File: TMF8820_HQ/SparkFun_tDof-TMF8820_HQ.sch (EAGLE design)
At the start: 24 parts, among them J4 QWIIC_RIGHT_ANGLE, J5 QWIIC_RIGHT_ANGLE

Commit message: Adds default address to HQ boards, fixes some clearance issues
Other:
- note added: "Default Addres: 0x41"
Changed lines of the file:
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@@
 <text x="58.42" y="165.1" size="1.778" layer="97" font="vector">VCC Range: 2.7V - 3.3V
 I/O VCC Range: 1.62V - 3.3V</text>
+<text x="83.82" y="111.76" size="1.778" layer="97" font="vector">Default Addres: 0x41</text>
 </plain>
 <instances>

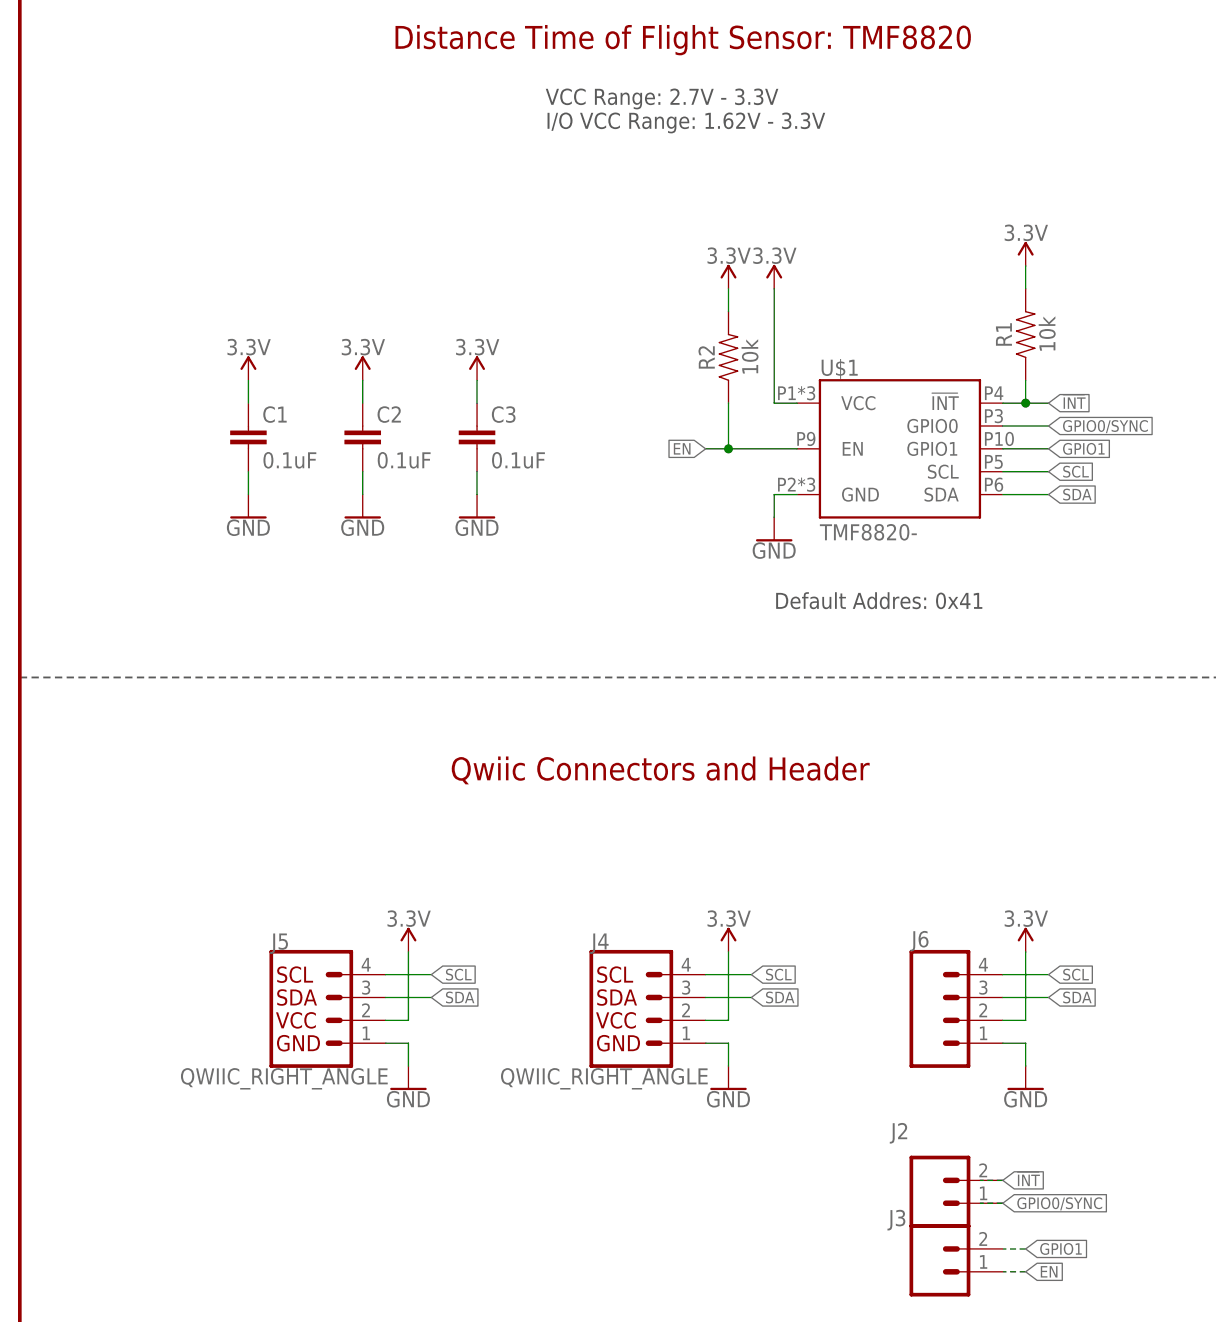
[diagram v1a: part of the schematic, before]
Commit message: Updates the TMF882X device in the library to have two variants of the two ICs
* Better silk labeling for the 8820 and 8820 HQ
* Adds new IC variants to both designs
* Adds default addresses to schematics
* Moves some traces and vias for better ground pour in the 8820 design
* Moves entire 8820 design to origin in board file
* Adds measure from center of qwiic connector to edge in 8820 design
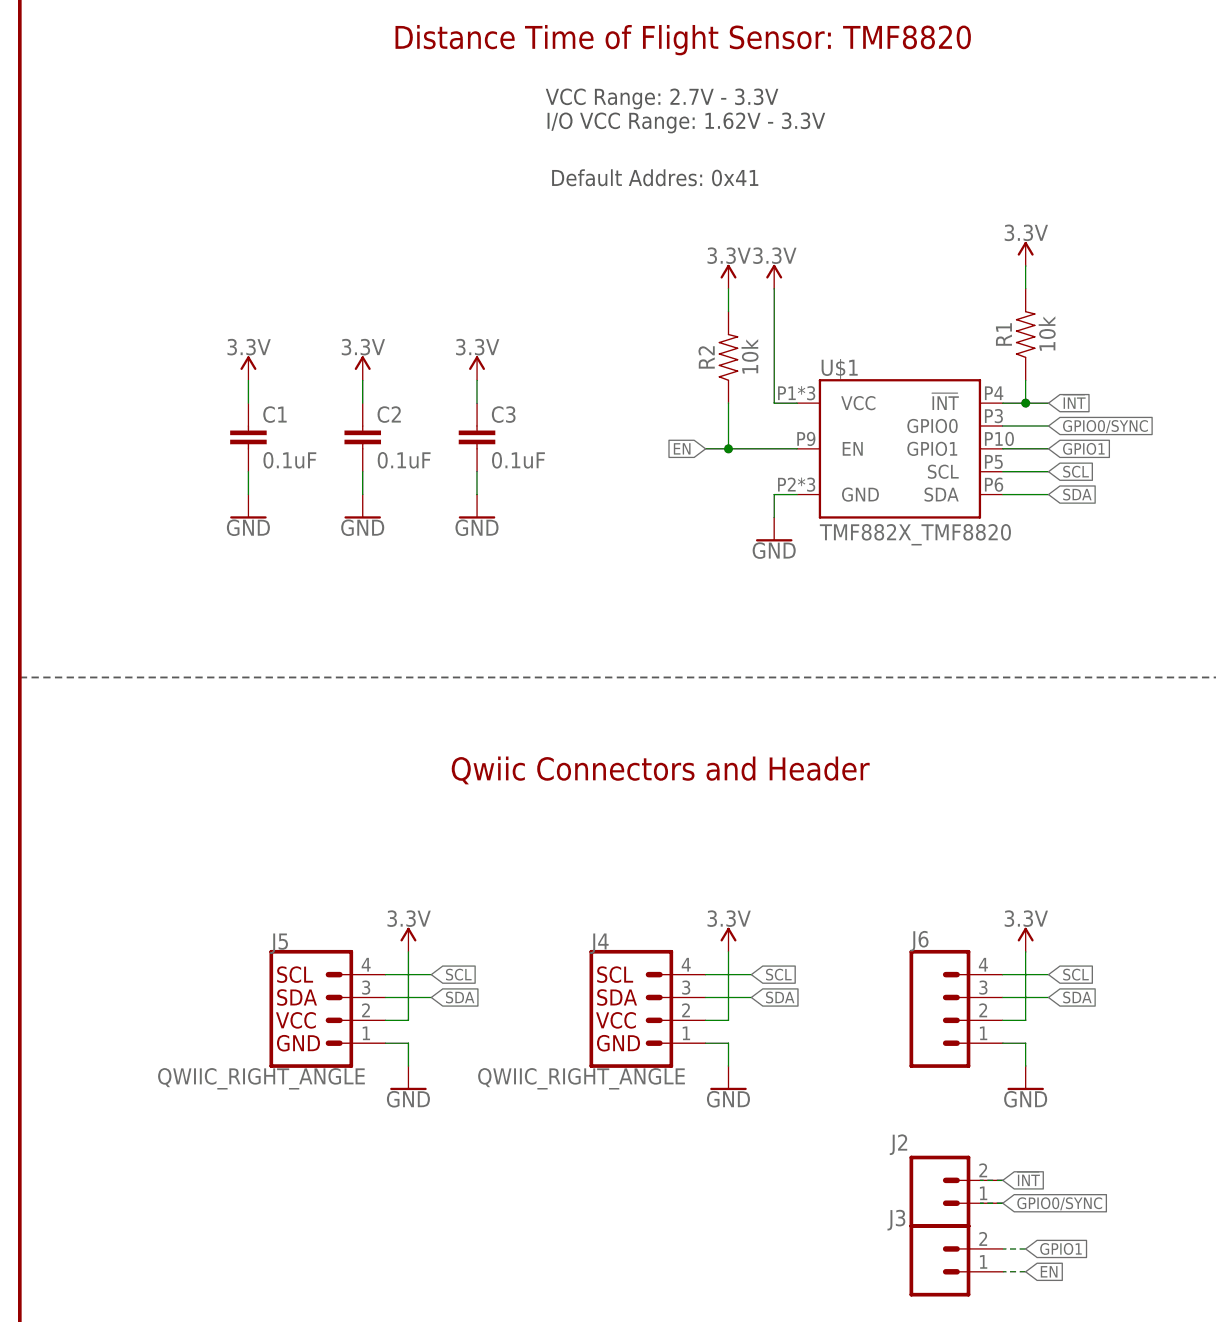
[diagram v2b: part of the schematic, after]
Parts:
- U$1: value TMF8820- -> TMF882X_TMF8820; device TMF882X:TMF8820- -> TMF882X:TMF882X_TMF8820
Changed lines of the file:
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@@
 <part name="I2C" library="SparkFun-Jumpers" deviceset="JUMPER-SMT_3_2-NC_TRACE" device="_SILK" package3d_urn="urn:adsk.eagle:package:39289/1" value="I2C_PU"/>
 <part name="SUPPLY10" library="SparkFun-PowerSymbols" deviceset="3.3V" device=""/>
-<part name="U$1" library="TMF882X" deviceset="TMF8820" device="-"/>
+<part name="U$1" library="TMF882X" deviceset="TMF882X" device="_TMF8820"/>
 <part name="C1" library="SparkFun-Capacitors" deviceset="0.1UF" device="-0402T-6.3V-10%-X7R" value="0.1uF"/>
 <part name="C2" library="SparkFun-Capacitors" deviceset="0.1UF" device="-0402T-6.3V-10%-X7R" value="0.1uF"/>
@@
 <text x="58.42" y="165.1" size="1.778" layer="97" font="vector">VCC Range: 2.7V - 3.3V
 I/O VCC Range: 1.62V - 3.3V</text>
-<text x="83.82" y="111.76" size="1.778" layer="97" font="vector">Default Addres: 0x41</text>
+<text x="58.928" y="158.75" size="1.778" layer="97" font="vector">Default Addres: 0x41</text>
 </plain>
 <instances>
@@
 <instance part="H8" gate="G$1" x="236.22" y="27.94" smashed="yes"/>
 <instance part="J4" gate="G$1" x="68.58" y="66.04" smashed="yes">
-<attribute name="VALUE" x="53.34" y="60.706" size="1.778" layer="96" font="vector" align="top-left"/>
+<attribute name="VALUE" x="50.8" y="60.706" size="1.778" layer="96" font="vector" align="top-left"/>
 <attribute name="NAME" x="63.5" y="73.914" size="1.778" layer="95" font="vector"/>
 </instance>
 <instance part="J5" gate="G$1" x="33.02" y="66.04" smashed="yes">
-<attribute name="VALUE" x="17.78" y="60.706" size="1.778" layer="96" font="vector" align="top-left"/>
+<attribute name="VALUE" x="15.24" y="60.706" size="1.778" layer="96" font="vector" align="top-left"/>
 <attribute name="NAME" x="27.94" y="73.914" size="1.778" layer="95" font="vector"/>
 </instance>
@@
 <instance part="J2" gate="G$1" x="101.6" y="45.72" smashed="yes">
 <attribute name="VALUE" x="99.06" y="40.894" size="1.778" layer="96" font="vector"/>
-<attribute name="NAME" x="96.774" y="52.832" size="1.778" layer="95" font="vector"/>
+<attribute name="NAME" x="96.774" y="51.562" size="1.778" layer="95" font="vector"/>
 </instance>
 <instance part="J3" gate="G$1" x="101.6" y="38.1" smashed="yes">

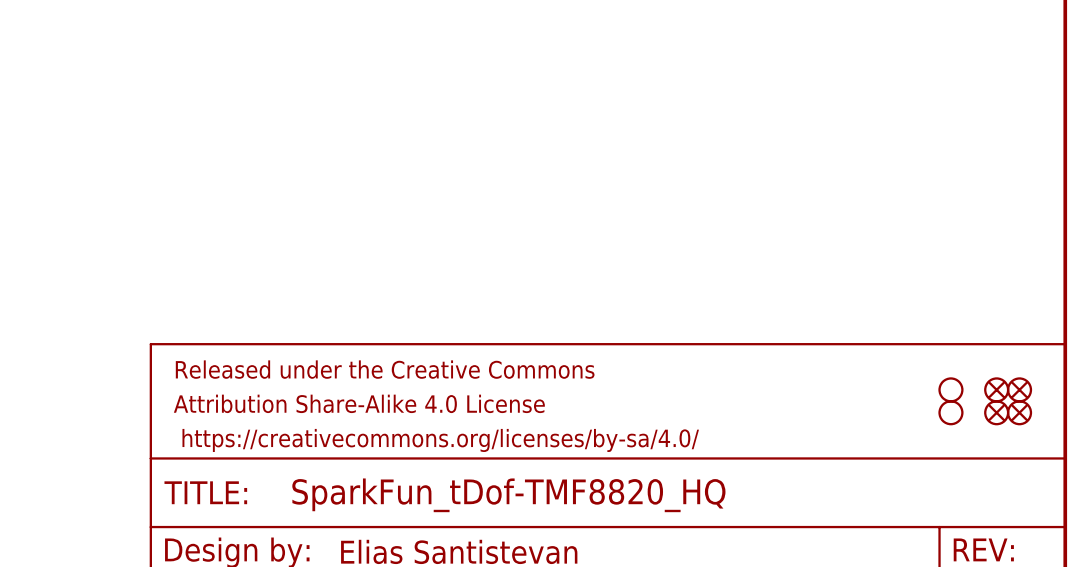
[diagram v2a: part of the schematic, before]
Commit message: Adds logos to schematic
* Moves measures to board (weren't moved when the design was put at the origin)
* Replaces IO1 silk with IO0 on GPIO0 PTH header
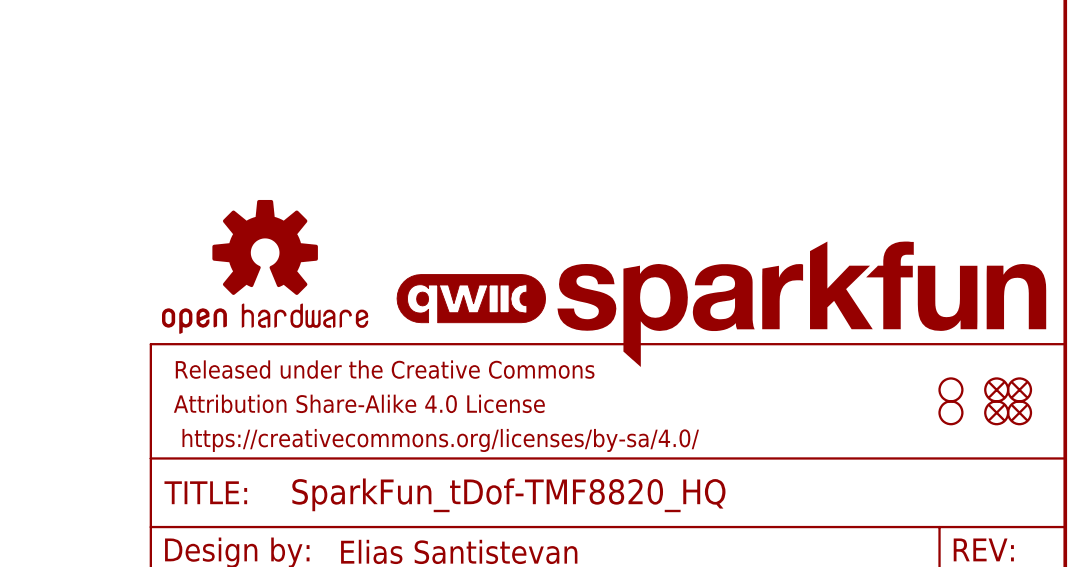
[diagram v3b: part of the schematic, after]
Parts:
- added LOGO1: SFE_LOGO_NAMEBLANK, SparkFun-Aesthetics:SFE_LOGO_NAMEBLANK
- added LOGO2: QWIIC_LOGO_3MM, SparkFun-Aesthetics:QWIIC_LOGO_3MM
- added LOGO3: OSHW-LOGONO_SILK, SparkFun-Aesthetics:OSHW-LOGONO_SILK
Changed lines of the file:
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@@
 <part name="J2" library="SparkFun-Connectors" deviceset="CONN_02" device="1X02_NO_SILK"/>
 <part name="J3" library="SparkFun-Connectors" deviceset="CONN_02" device="1X02_NO_SILK"/>
+<part name="LOGO1" library="SparkFun-Aesthetics" deviceset="SFE_LOGO_NAME" device="BLANK"/>
+<part name="LOGO2" library="SparkFun-Aesthetics" deviceset="QWIIC_LOGO" device="_3MM"/>
+<part name="LOGO3" library="SparkFun-Aesthetics" deviceset="OSHW-LOGO" device="NO_SILK"/>
 </parts>
 <sheets>
@@
 <attribute name="NAME" x="96.52" y="43.18" size="1.778" layer="95" font="vector"/>
 </instance>
+<instance part="LOGO1" gate="G$1" x="190.5" y="33.02" smashed="yes"/>
+<instance part="LOGO2" gate="G$1" x="182.88" y="40.64" smashed="yes"/>
+<instance part="LOGO3" gate="G$1" x="160.02" y="45.72" smashed="yes"/>
 </instances>
 <busses>

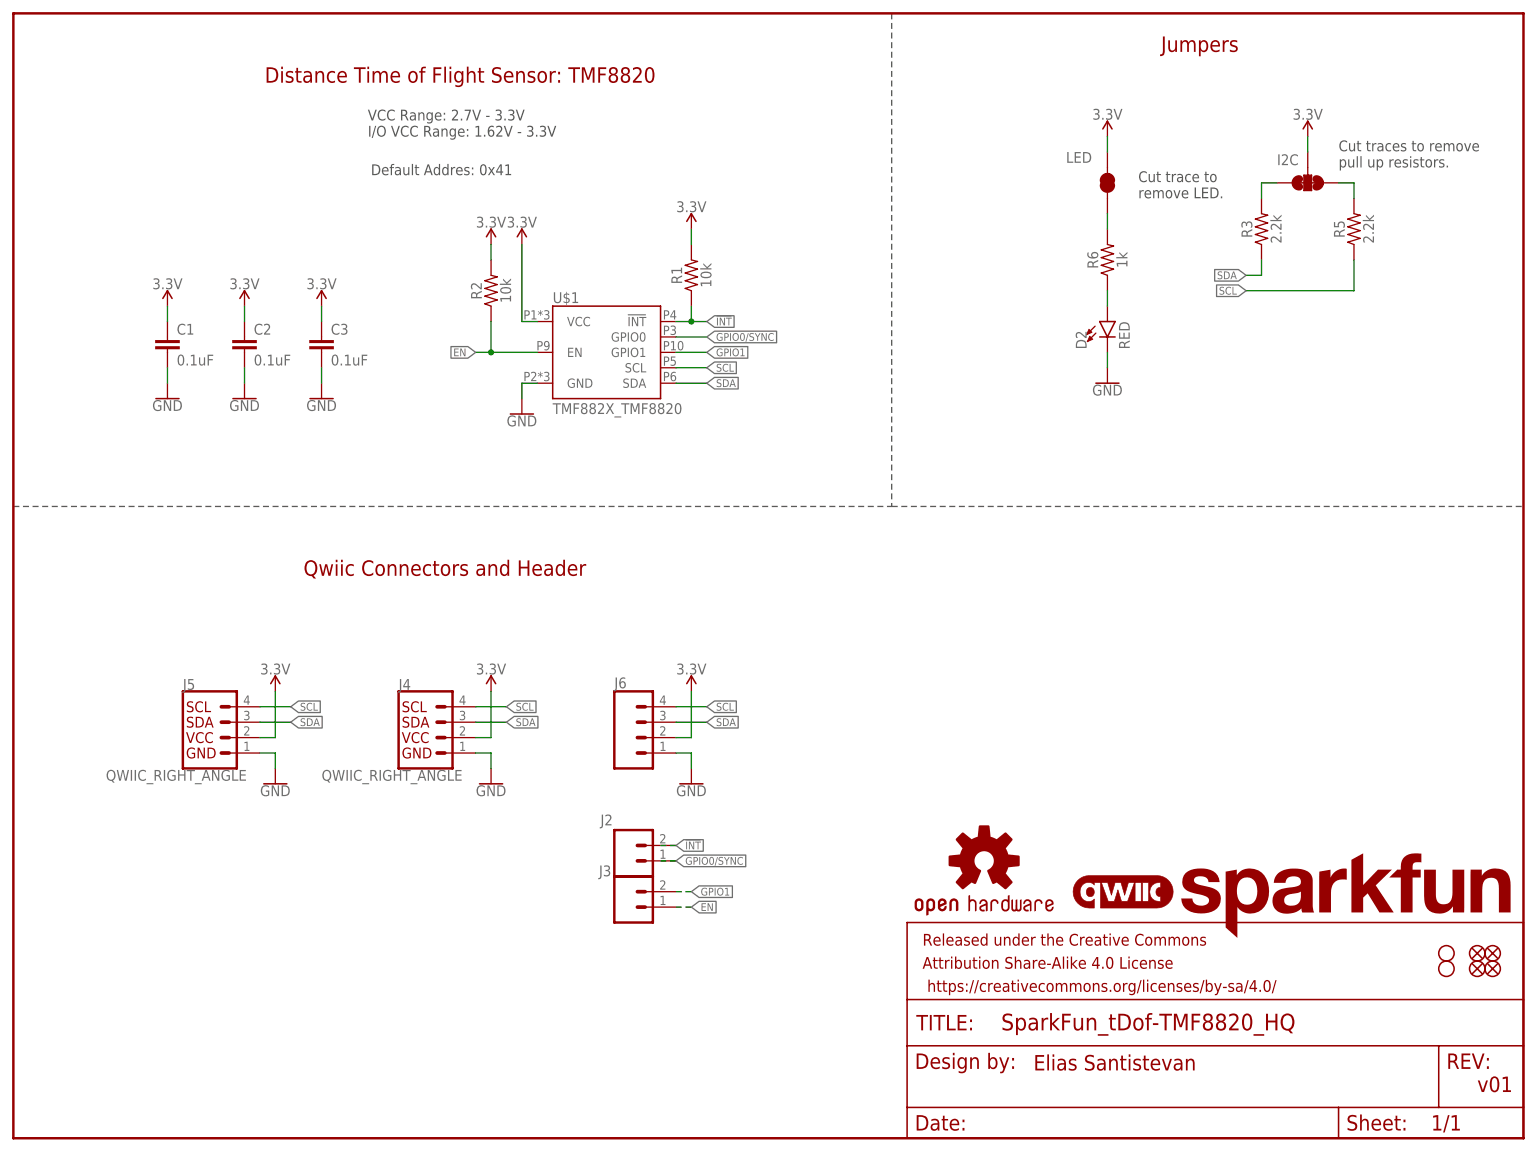
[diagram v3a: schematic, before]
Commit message: Moves the IC on the SparkFun "HQ" design to one side
* All other parts are on the other side. This makes room for product selection boxes so that one PCB can be used for both.
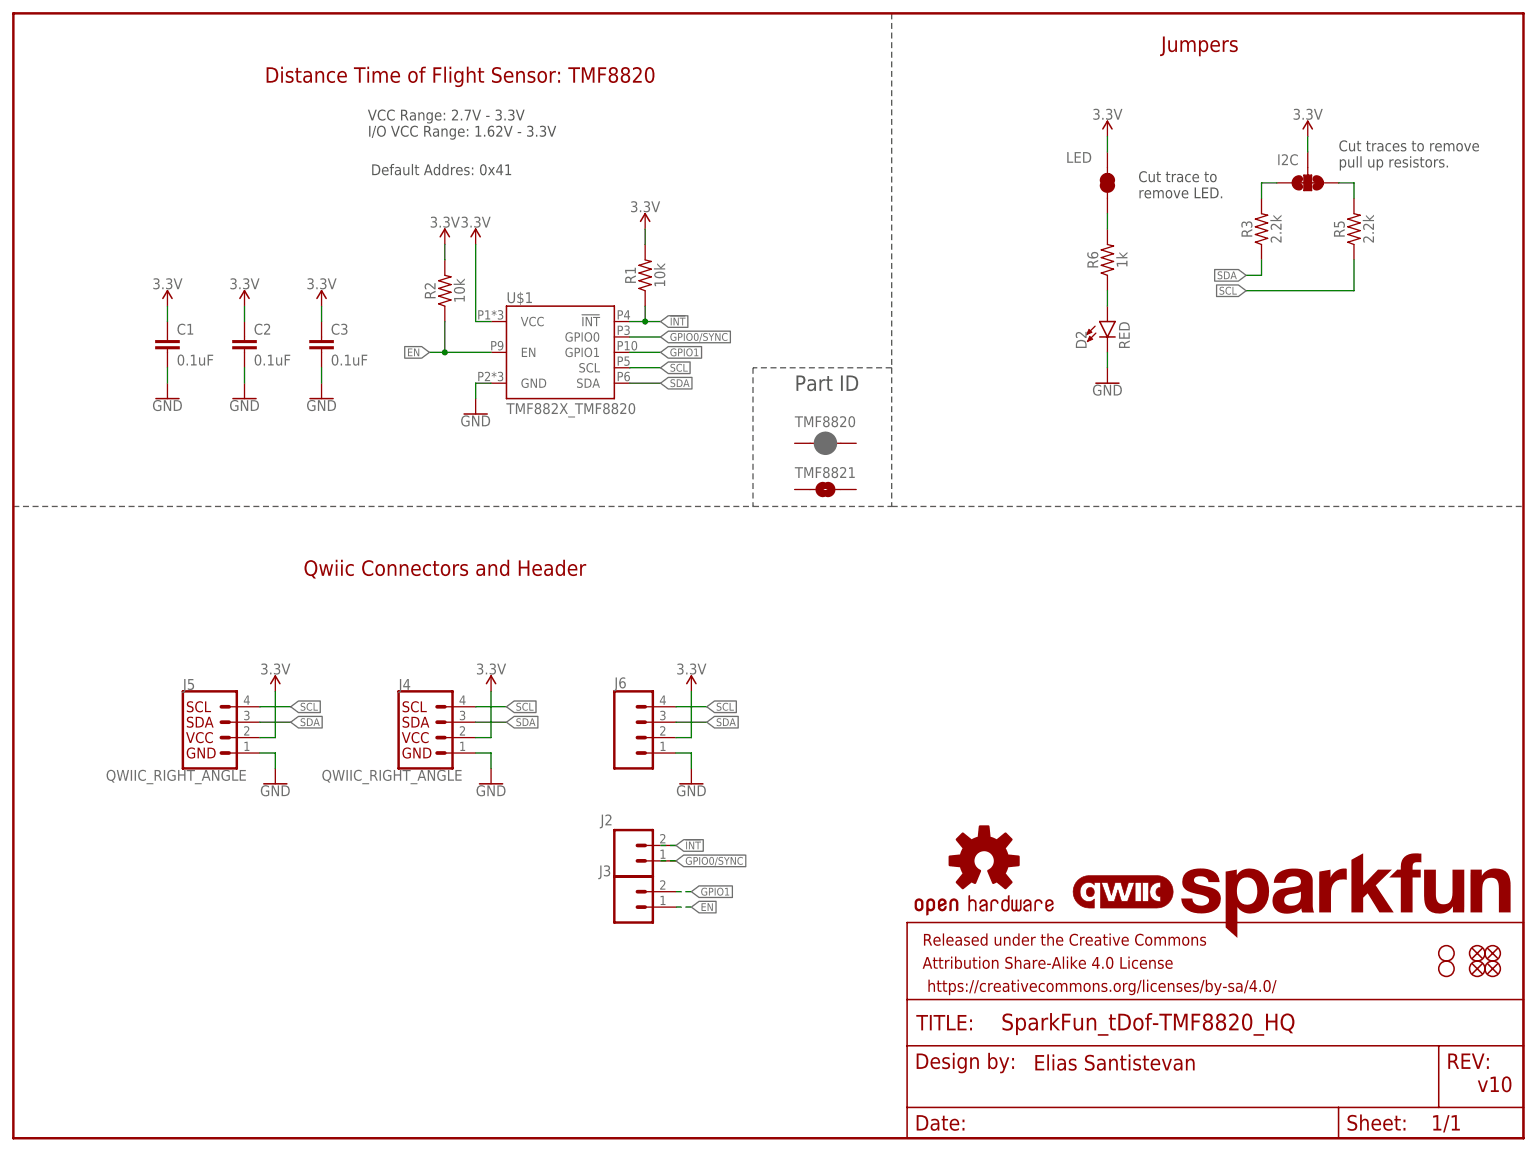
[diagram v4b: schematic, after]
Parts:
- added TMF8820: JUMPER-SMT_2_NC_PASTE_SILK, SparkFun-Jumpers:JUMPER-SMT_2_NC_PASTE_SILK
- added TMF8821: JUMPER-SMT_2_NO_SILK, SparkFun-Jumpers:JUMPER-SMT_2_NO_SILK
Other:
- note added: "Part ID"
- note added: "v10"
- note removed: "v01"
- moved on the sheet: R1, R2, U$1
